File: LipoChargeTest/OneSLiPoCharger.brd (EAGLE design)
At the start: 86.4 x 52.1 mm, 58 parts, among them IC1 LM358N, Q1 BUZ10

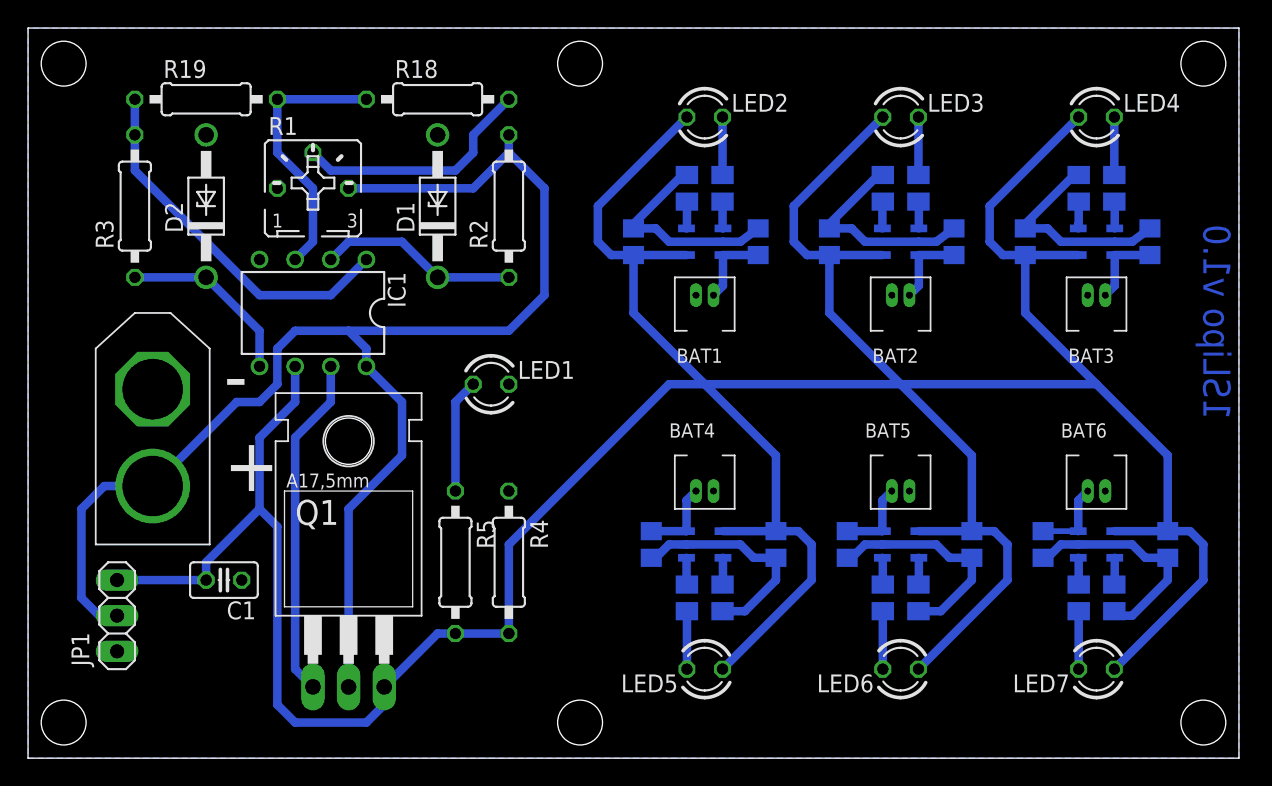
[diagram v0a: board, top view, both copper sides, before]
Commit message: Add lipo charger test circuits
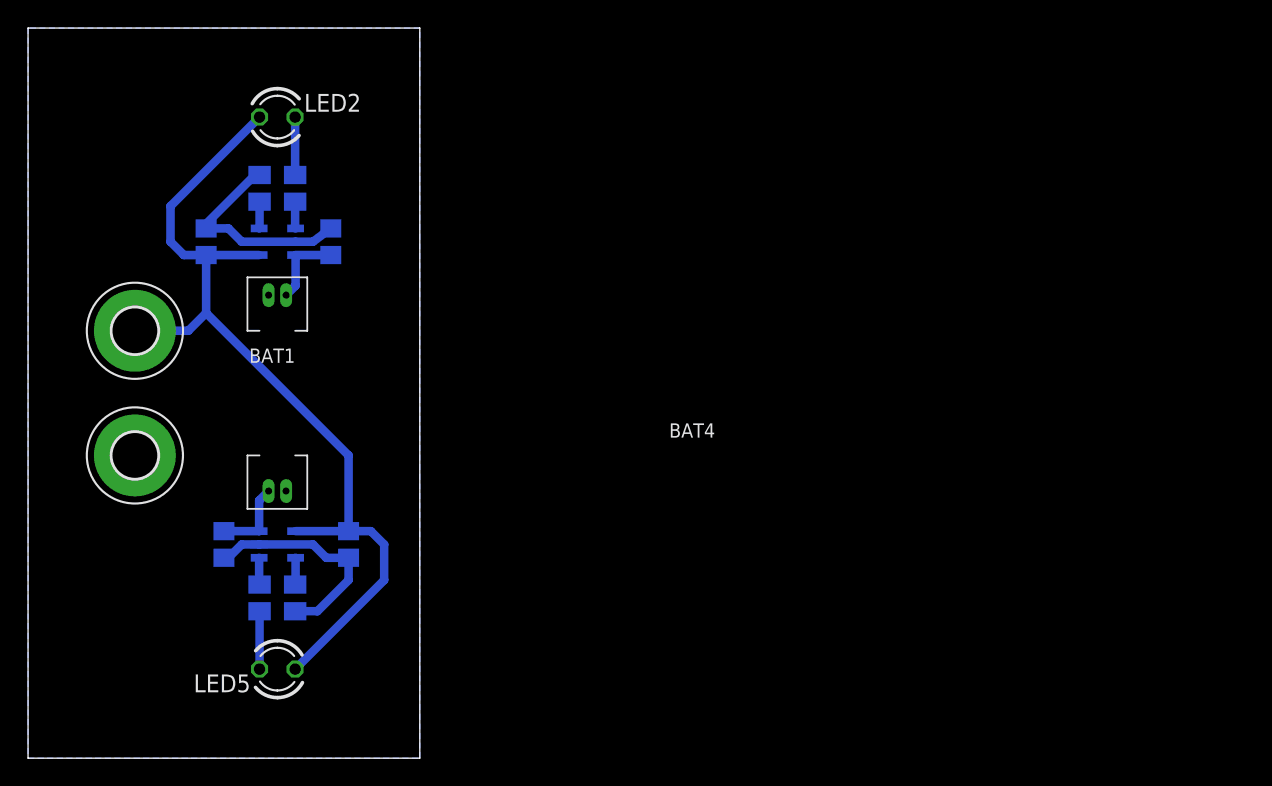
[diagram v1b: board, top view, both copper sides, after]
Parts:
- removed C1: (no value), rcl:C025-025X050
- removed C10, C11, C12, C13, C4, C5, C6, C7: 4.7uF, rcl:C0805
- removed D1, D2: 1N4728, diode:DO41Z10
- removed IC1: LM358N, linear:DIL08
- removed JP1: (no value), pinhead:1X03
- removed LED1, LED3, LED4, LED6, LED7: (no value), led:LED3MM
- removed Q1: BUZ10, transistor-fet:TO220
- removed R1: (no value), pot:B25P
- removed R10, R14, R16, R8: (no value), rcl:M0805
- removed R11, R15, R17, R9: 3.9k, rcl:M0805
- removed R18, R2: 1K, rcl:0207/10
- removed R19: 470K, rcl:0207/10
- removed R3: 10K, rcl:0207/10
- removed R4, R5: 4.7K, rcl:0207/10
- removed U$10, U$12, U$4, U$6: MCP73831, MCP73831:MCP73831-SOT23
- removed U$11, U$13, U$5, U$7: PICOBLADE-2PIN, Picoblade:PICOBLADE-2PIN
- removed U$3: XT60, XTConnector:XT60
- added H1, H2: MOUNT-PAD-ROUND3.3, holes:3,3-PAD
- moved C8 30.5 mm to (22.9, 15.2)
- moved C9 30.5 mm to (14.0, 15.2)
- moved C2 30.5 mm to (12.7, 36.8)
- moved C3 30.5 mm to (21.6, 36.8)
- moved R12 30.5 mm to (16.5, 11.4)
- moved R13 30.5 mm to (19.1, 11.4)
- moved R6 30.5 mm to (19.1, 40.6)
- moved R7 30.5 mm to (16.5, 40.6)
- moved LED2 30.5 mm to (17.8, 45.7)
- moved LED5 30.5 mm to (17.8, 6.35)
- moved U$1 30.5 mm to (17.8, 36.8)
- moved U$2 30.5 mm to (17.8, 33.0)
- moved U$8 30.5 mm to (17.8, 15.2)
- moved U$9 30.5 mm to (17.8, 19.1)
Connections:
- removed net N$1: R1.S, R18.2
- removed net N$10: LED1.A, R5.1
- removed net N$11: LED3.K, R8.2
- removed net N$12: R8.1, U$4.1
- removed net N$13: R9.2, U$4.5
- removed net N$14: C5.2, U$4.3, U$5.P$2
- removed net N$15: LED4.K, R10.2
- removed net N$16: R10.1, U$6.1
- removed net N$17: R11.2, U$6.5
- removed net N$18: C7.2, U$6.3, U$7.P$2
- removed net N$2: D2.C, IC1.5, R3.1
- removed net N$23: LED6.K, R14.2
- removed net N$24: R14.1, U$10.1
- removed net N$25: R15.2, U$10.5
- removed net N$26: C11.2, U$10.3, U$11.P$2
- removed net N$27: LED7.K, R16.2
- removed net N$28: R16.1, U$12.1
- removed net N$29: R17.2, U$12.5
- removed net N$3: D1.C, IC1.2, R2.1
- removed net N$30: C13.2, U$12.3, U$13.P$2
- removed net N$31: IC1.3, R18.1, R19.2
- removed net N$4: IC1.1, R19.1, R3.2
- removed net N$5: IC1.7, Q1.1
- removed net VCC: IC1.8, JP1.2, Q1.2, R1.E, R2.2, U$3.POS
- net +5V: now also H1.B3,3; no longer C1.2, C10.1, C12.1, C4.1, C6.1, IC1.6, JP1.1, LED3.A, LED4.A, LED6.A, LED7.A, Q1.3, R4.2, R5.2, U$10.4, U$12.4, U$4.4, U$6.4
- net GND: now also H2.B3,3; no longer C1.1, C10.2, C11.1, C12.2, C13.1, C4.2, C5.1, C6.2, C7.1, D1.A, D2.A, IC1.4, JP1.3, LED1.K, R1.A, R11.1, R15.1, R17.1, R4.1, R9.1, U$10.2, U$11.P$1, U$12.2, U$13.P$1, U$3.NEG, U$4.2, U$5.P$1, U$6.2, U$7.P$1
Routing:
- net +5V: track 293.2 -> 66.0 mm
- net VCC: track 103.8 -> 0.00 mm
- net GND: track 94.4 -> 31.2 mm
- net N$4: track 26.3 -> 0.00 mm
- net N$5: track 24.4 -> 0.00 mm
- net N$31: track 19.4 -> 0.00 mm
- net N$1: track 17.3 -> 0.00 mm
- net N$3: track 14.3 -> 0.00 mm
- net N$2: track 13.0 -> 0.00 mm
- net N$10: track 8.15 -> 0.00 mm
- net N$14: track 5.97 -> 0.00 mm
- net N$18: track 5.65 -> 0.00 mm
- net N$30: track 5.65 -> 0.00 mm
- net N$26: track 5.65 -> 0.00 mm
- net N$27: track 4.13 -> 0.00 mm
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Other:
- board size 86.4 x 52.1 mm -> 27.9 x 52.1 mm
- board text removed: "1SLipo v1.0"
- board text removed: "BAT2"
- board text removed: "BAT3"
- board text removed: "BAT5"
- board text removed: "BAT6"
